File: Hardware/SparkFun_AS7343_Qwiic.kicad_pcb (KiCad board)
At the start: 2 copper layers, 25.4 x 25.4 mm, 65 parts, among them J1 Qwiic_RA, J2 Qwiic_RA, J3 Conn_01x06, Q1 BSS138, Q2 BSS138, U1 RT9080-1.8V, U2 AS7343

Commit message: I2C address in sch and bottom silk
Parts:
- added kibuzzard-67F027E1: G***, kibuzzard-67F027E1, B.Cu at (132.4, 102.3)

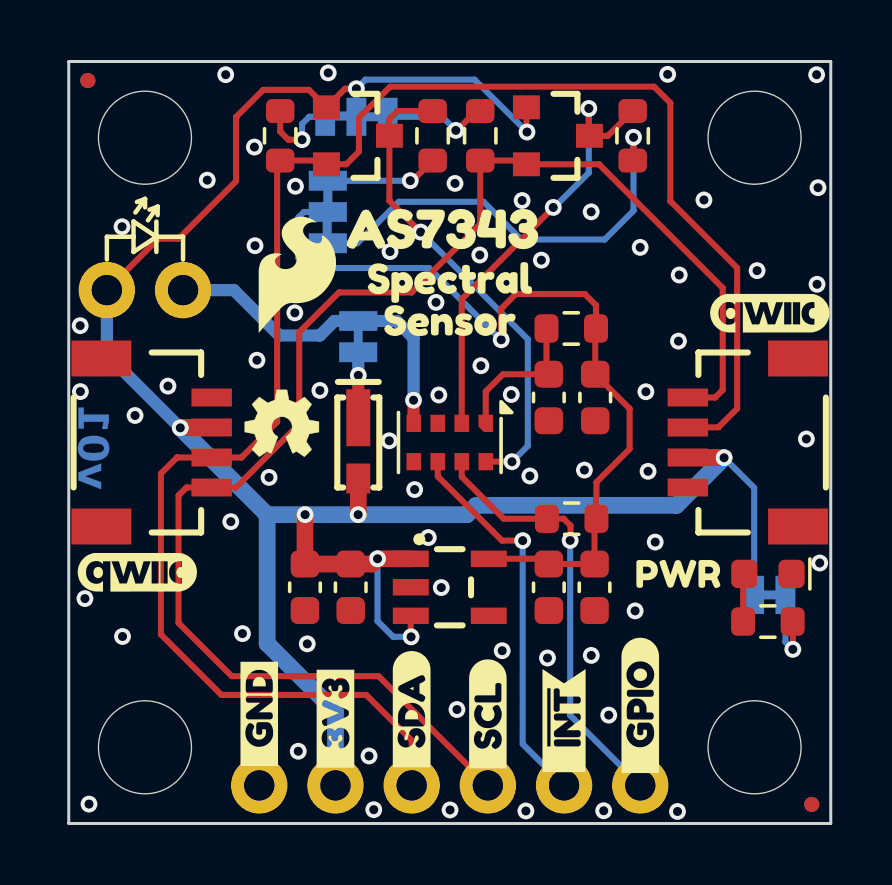
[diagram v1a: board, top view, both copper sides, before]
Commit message: checklist run eng
-sch tightening
-vcc range added to sch
-removed PROD_ID from DNP LED
-add 1.8V testpoint
-increased copper to dimension clearance from 3 mils to 8 mils (avoiding sanding damage)
-nudged qwiic connectors inward from the edge by 5mils (avoiding sanding damage)
-updated pin one marker on IC from triangle to dot
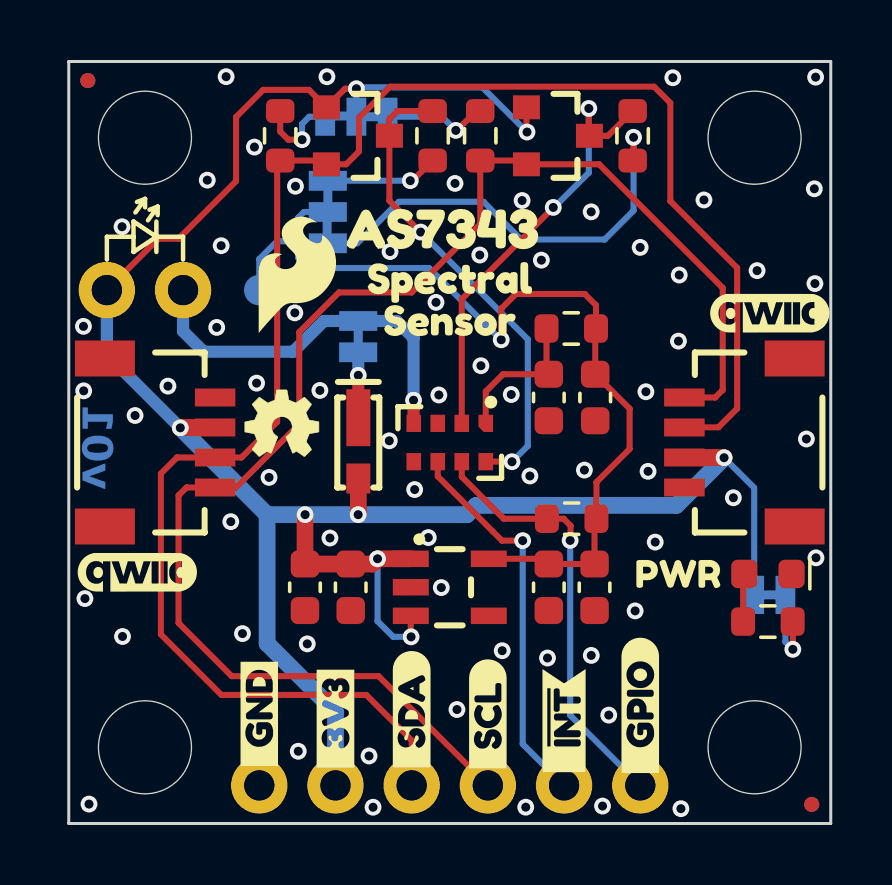
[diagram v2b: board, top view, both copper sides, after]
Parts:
- added TP1: 1.0mm, SparkFun-Connector:TestPoint-1.0mm, B.Cu at (129.6, 93.0)
- moved J1 0.12 mm to (143.8, 98.1)
- moved J2 0.12 mm to (128.1, 98.1)
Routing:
- net 1V8: track 28.0 -> 30.6 mm
- net Net-(D3-K): track 11.6 -> 12.8 mm
- net GND: vias 64 -> 66

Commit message: measures
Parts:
- moved D1 0.44 mm to (146.1, 102.5)
- moved R3 0.44 mm to (146.1, 104.1)
- moved kibuzzard-65A8A8B4 0.19 mm to (143.4, 102.4)
